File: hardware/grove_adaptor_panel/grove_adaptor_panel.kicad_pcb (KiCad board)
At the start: 2 copper layers, 64 x 41.5 mm, 65 parts, among them J1 Conn_01x04, J2 Conn_01x04

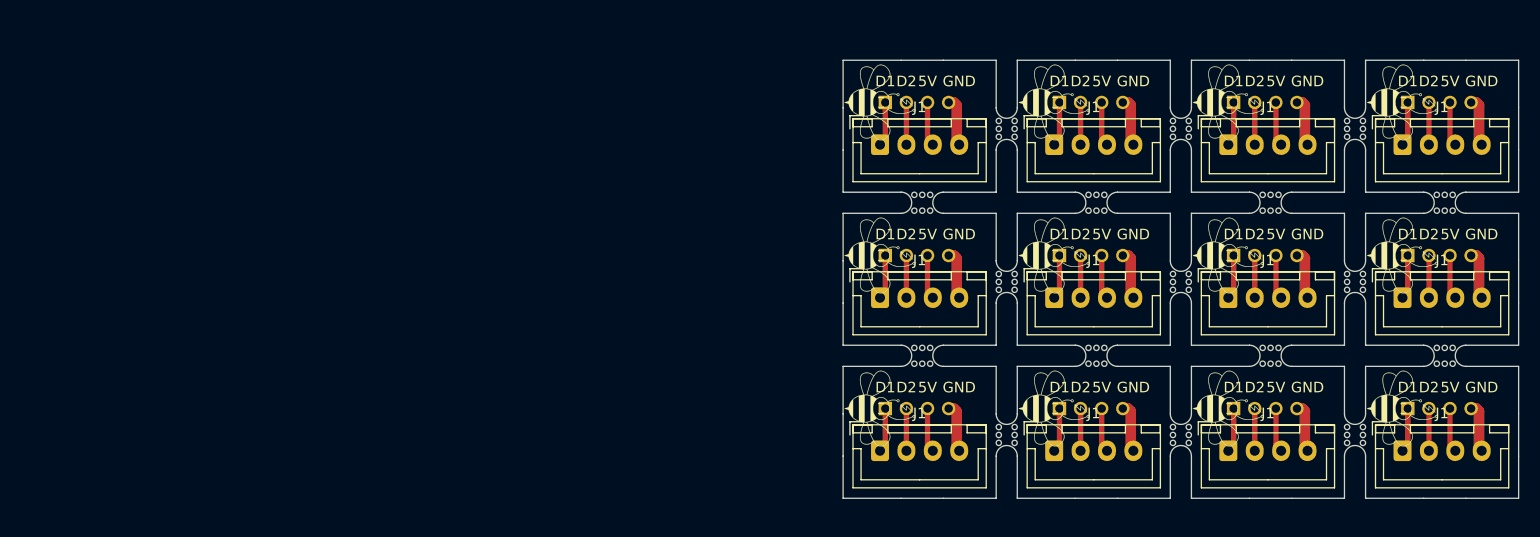
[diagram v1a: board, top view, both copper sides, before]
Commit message: update grove panel to comply with manufacturer request
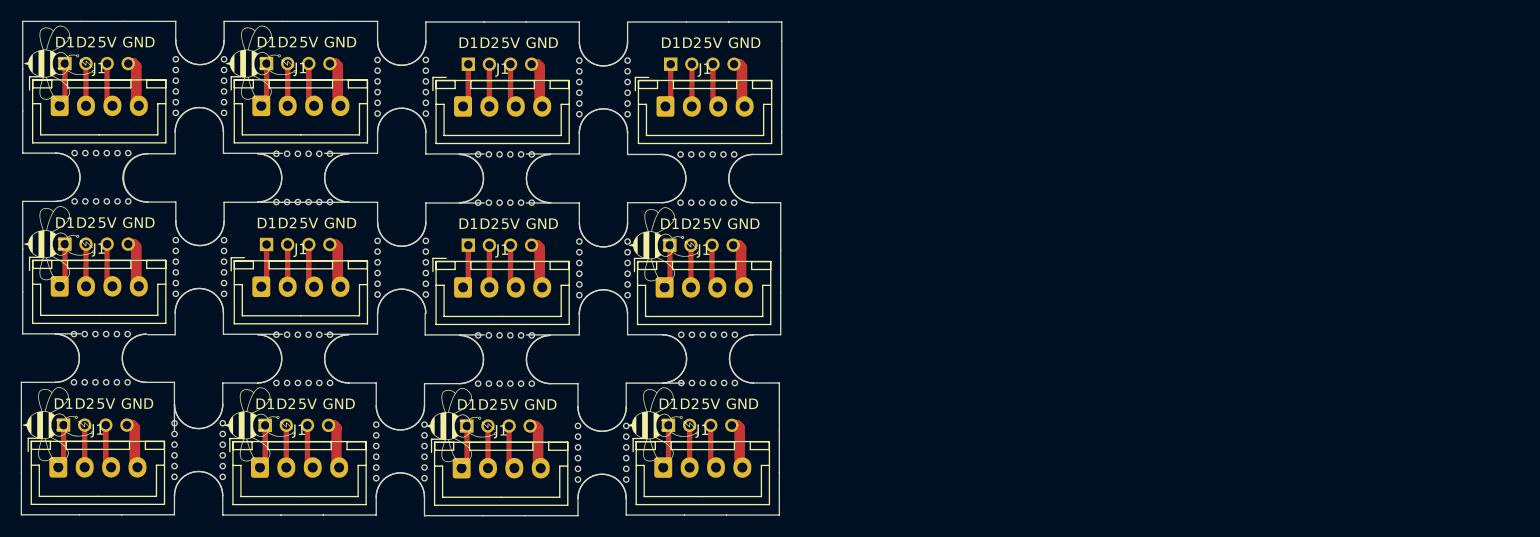
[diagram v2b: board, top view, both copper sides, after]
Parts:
- removed the G*** at (209.0, 93.5)
- removed the G*** at (176.0, 122.5)
- removed the G*** at (225.5, 108.0)
- removed the G*** at (209.0, 108.0)
- removed the G*** at (192.5, 108.0)
- removed the J1 at (209.0, 97.5)
- removed the J1 at (176.0, 126.5)
- removed the J1 at (225.5, 112.0)
- removed the J1 at (209.0, 112.0)
- removed the J1 at (192.5, 112.0)
- removed the J2 at (212.5, 93.5)
- removed the J2 at (179.5, 122.5)
- removed the J2 at (229.0, 108.0)
- removed the J2 at (212.5, 108.0)
- removed the J2 at (196.0, 108.0)
- removed the U$3 at (217.5, 94.0)
- removed the U$3 at (184.5, 123.0)
- removed the U$3 at (234.0, 108.5)
- removed the U$3 at (217.5, 108.5)
- removed the U$3 at (201.0, 108.5)
- removed mouse-bite-2mm-slot (x17): VAL**, Panelization:mouse-bite-2mm-slot
- added G***: LOGO, logo-beehive:logo-beehive-7_2х6_7mm, F.Cu at (98.1, 124.1)
- added J1: Conn_01x04, Connector_JST:JST_XH_B4B-XH-A_1x04_P2.50mm_Vertical, F.Cu at (136.5, 111.0)
- added J1: Conn_01x04, Connector_JST:JST_XH_B4B-XH-A_1x04_P2.50mm_Vertical, F.Cu at (155.7, 93.9)
- added J1: Conn_01x04, Connector_JST:JST_XH_B4B-XH-A_1x04_P2.50mm_Vertical, F.Cu at (136.5, 93.9)
- added J1: Conn_01x04, Connector_JST:JST_XH_B4B-XH-A_1x04_P2.50mm_Vertical, F.Cu at (117.4, 111.0)
- added J1: Conn_01x04, Connector_JST:JST_XH_B4B-XH-A_1x04_P2.50mm_Vertical, F.Cu at (98.1, 128.1)
- added J2: Conn_01x04, Grove-Gas Sensor v1.4:4P-LEADED-2.0, B.Cu at (140.0, 107.0)
- added J2: Conn_01x04, Grove-Gas Sensor v1.4:4P-LEADED-2.0, B.Cu at (159.2, 89.9)
- added J2: Conn_01x04, Grove-Gas Sensor v1.4:4P-LEADED-2.0, B.Cu at (140.0, 89.9)
- added J2: Conn_01x04, Grove-Gas Sensor v1.4:4P-LEADED-2.0, B.Cu at (120.9, 107.0)
- added J2: Conn_01x04, Grove-Gas Sensor v1.4:4P-LEADED-2.0, B.Cu at (101.6, 124.1)
- added U$3: , Grove-Gas Sensor v1.4:TWIGLOGO, B.Cu at (106.6, 124.6)
- added mouse-bite-5mm-slot: VAL**, panelization:mouse-bite-5mm-slot, F.Cu at (159.6, 100.7)
- added mouse-bite-5mm-slot: VAL**, panelization:mouse-bite-5mm-slot, F.Cu at (149.7, 126.7)
- added mouse-bite-5mm-slot: VAL**, panelization:mouse-bite-5mm-slot, F.Cu at (102.2, 117.7)
- added mouse-bite-5mm-slot: VAL**, panelization:mouse-bite-5mm-slot, F.Cu at (111.4, 126.4)
- added mouse-bite-5mm-slot: VAL**, panelization:mouse-bite-5mm-slot, F.Cu at (130.6, 126.6)
- added mouse-bite-5mm-slot: VAL**, panelization:mouse-bite-5mm-slot, F.Cu at (121.4, 100.6)
- added mouse-bite-5mm-slot: VAL**, panelization:mouse-bite-5mm-slot, F.Cu at (102.2, 100.6)
- added mouse-bite-5mm-slot: VAL**, panelization:mouse-bite-5mm-slot, F.Cu at (111.6, 91.9)
- added mouse-bite-5mm-slot: VAL**, panelization:mouse-bite-5mm-slot, F.Cu at (130.7, 92.0)
- added mouse-bite-5mm-slot: VAL**, panelization:mouse-bite-5mm-slot, F.Cu at (149.8, 109.2)
- added mouse-bite-5mm-slot: VAL**, panelization:mouse-bite-5mm-slot, F.Cu at (140.5, 117.9)
- added mouse-bite-5mm-slot: VAL**, panelization:mouse-bite-5mm-slot, F.Cu at (149.8, 92.1)
- added mouse-bite-5mm-slot: VAL**, panelization:mouse-bite-5mm-slot, F.Cu at (140.5, 100.7)
- added mouse-bite-5mm-slot: VAL**, panelization:mouse-bite-5mm-slot, F.Cu at (130.7, 109.2)
- added mouse-bite-5mm-slot: VAL**, panelization:mouse-bite-5mm-slot, F.Cu at (121.4, 117.8)
- added mouse-bite-5mm-slot: VAL**, panelization:mouse-bite-5mm-slot, F.Cu at (111.6, 109.1)
- added mouse-bite-5mm-slot: VAL**, panelization:mouse-bite-5mm-slot, F.Cu at (159.7, 117.8)
- moved G*** 77.8 mm to (98.3, 89.8)
- moved J1 77.8 mm to (98.3, 93.8)
- moved J2 77.8 mm to (101.8, 89.8)
- moved U$3 77.8 mm to (106.8, 90.3)
- moved G*** 77.7 mm to (98.3, 106.9)
- moved J1 77.7 mm to (98.3, 110.9)
- moved J2 77.7 mm to (101.8, 106.9)
- moved U$3 77.7 mm to (106.8, 107.4)
- moved G*** 75.3 mm to (117.3, 124.1)
- moved J1 75.3 mm to (117.3, 128.1)
- moved J2 75.3 mm to (120.8, 124.1)
- moved U$3 75.3 mm to (125.8, 124.6)
- moved G*** 75.2 mm to (117.4, 89.8)
- moved J1 75.2 mm to (117.4, 93.8)
- moved J2 75.2 mm to (120.9, 89.8)
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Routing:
- net (no net): track 0.00 -> 85.6 mm
- net GND: track 56.5 -> 32.9 mm
- net +5V: track 50.5 -> 29.4 mm
- net Net-(J1-Pad1): track 50.5 -> 29.4 mm
- net Net-(J1-Pad2): track 48.0 -> 28.0 mm
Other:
- board size 64 x 41.5 mm -> 72 x 46.8 mm
